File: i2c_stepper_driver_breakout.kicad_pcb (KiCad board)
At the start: 2 copper layers, 13 parts, among them J1 Conn_01x10, J2 Conn_01x10, J3 S4B-PH-SM4-TB, U1 PCA9629A, U2 A3909

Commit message: Continued layout
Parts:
- added U3: MAX17291, Locator_Footprints:MAX17291ATA+T, F.Cu at (140.8, 96.6)
- J1, J2: moved to B.Cu
- J3: value S4B-PH-SM4-TB -> B4B-PH-K-S; footprint Connector_JST:JST_PH_B4B-PH-K_1x04_P2.00mm_Vertical -> Locator_Footprints:JST_PH_S4B-PH-SM4-TB_1x04-1MP_P2.00mm_Horizontal; moved to B.Cu
- R1, R2: value 10K -> DNP
- U2: footprint Package_SO:MSOP-10-1EP_3x3mm_P0.5mm_EP1.73x1.98mm_ThermalVias -> Locator_Footprints:A3909
- moved R4 33.0 mm to (141.0, 103.8)
- moved R2 31.3 mm to (144.3, 109.5)
- moved C3 31.3 mm to (147.2, 109.5)
- moved R1 31.3 mm to (141.4, 109.5)
- moved C2 29.0 mm to (151.6, 105.5)
- moved C4 29.0 mm to (151.6, 108.5)
- moved C1 27.8 mm to (151.0, 92.6)
- moved R3 27.8 mm to (151.0, 90.6)
- moved J2 22.4 mm to (156.0, 108.3)
- moved J3 3.86 mm to (146.5, 88.2)
- moved U1 2.62 mm to (146.3, 104.2)
- moved U2 1.32 mm to (146.5, 94.4)
- moved J1 1.20 mm to (137.0, 85.4), turned to 180 degrees
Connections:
- J1 pad 1: Net-(J1-Pad1) -> GND
- J1 pad 10: Net-(J1-Pad10) -> GND
- J2 pad 1: Net-(J2-Pad1) -> GND
- J2 pad 10: Net-(J2-Pad10) -> GND
- U2 pad 11: (no net) -> GND
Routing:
- net /OUT3: track 0.00 -> 10.7 mm, vias 0 -> 2
- net /OUT2: track 0.00 -> 9.38 mm, vias 0 -> 2
- net /OUT1: track 0.00 -> 2.00 mm, vias 0 -> 2
- net /OUT4: track 0.00 -> 1.96 mm, vias 0 -> 2
- added copper zone on B.Cu, net GND
- added copper zone on F.Cu, net GND
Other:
- board outline added: 23 x 28 mm
- rule via_min_drill: 0.3 -> 0.2

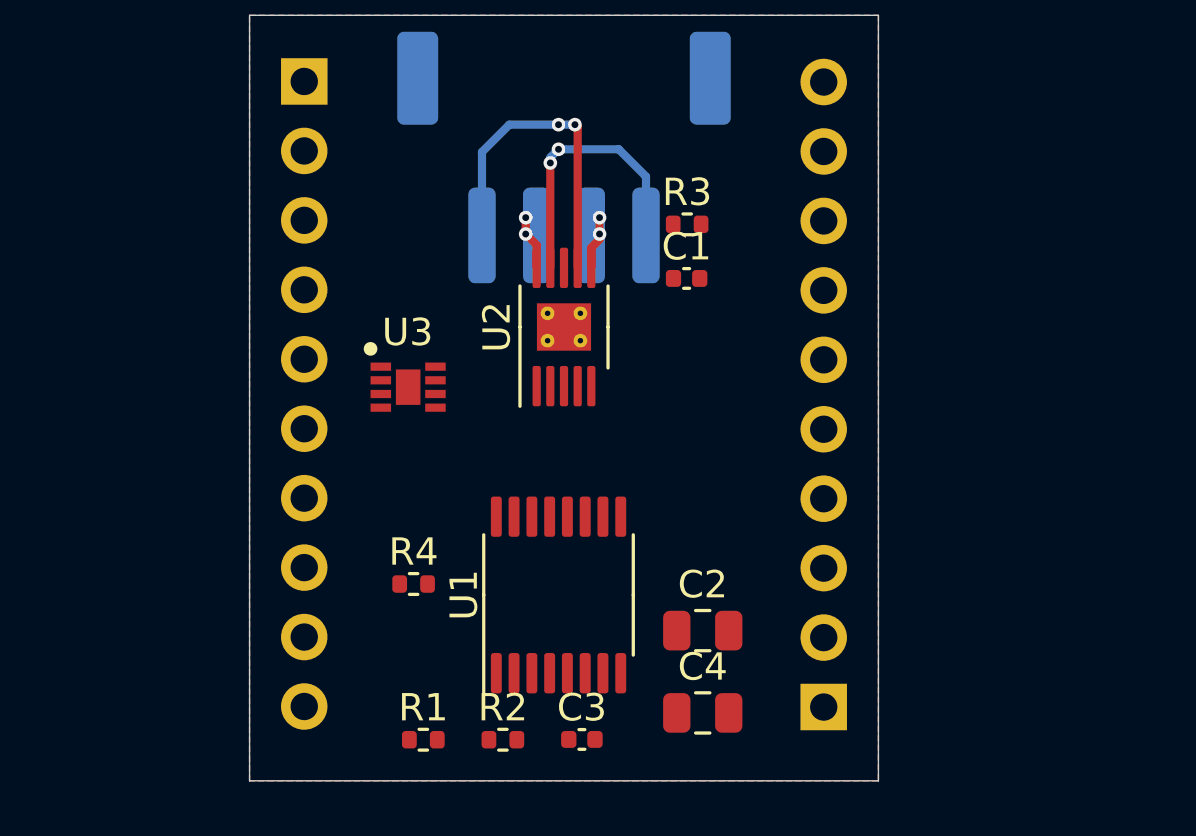
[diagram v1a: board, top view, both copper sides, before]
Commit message: Added boost converter, continued layout
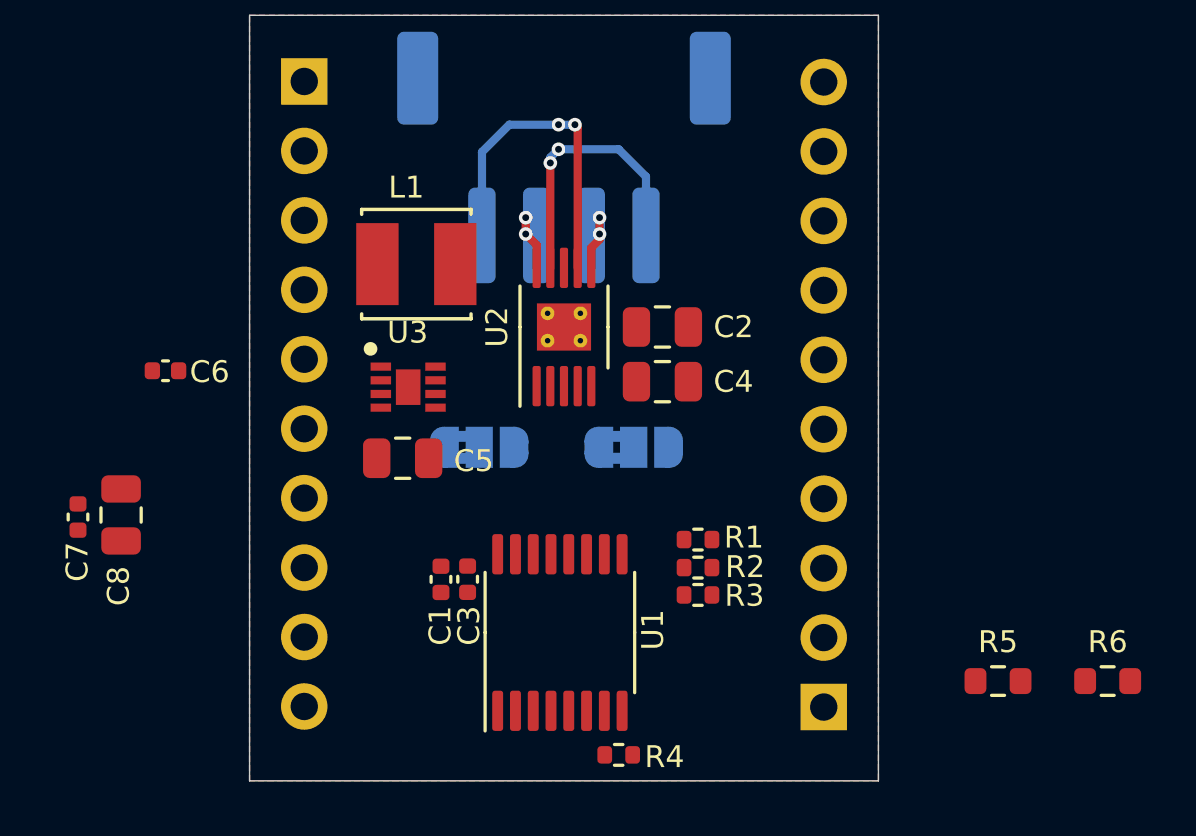
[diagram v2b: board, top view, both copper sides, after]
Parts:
- added C5: 22uF, Capacitor_SMD:C_0805_2012Metric, F.Cu at (140.6, 99.2)
- added C6: 1nF, Capacitor_SMD:C_0402_1005Metric, F.Cu at (131.9, 96.0)
- added C7: 100nF, Capacitor_SMD:C_0402_1005Metric, F.Cu at (128.7, 101.3)
- added C8: 22uF, Capacitor_SMD:C_0805_2012Metric, F.Cu at (130.3, 101.3)
- added JP1: VBB_Selection, Jumper:SolderJumper-3_P1.3mm_Bridged2Bar12_RoundedPad1.0x1.5mm, B.Cu at (143.4, 98.8)
- added JP2: VBB_Selection, Jumper:SolderJumper-3_P1.3mm_Bridged2Bar12_RoundedPad1.0x1.5mm, B.Cu at (149.1, 98.8)
- added L1: 4.7uH, Locator_Footprints:L_LQH44P, F.Cu at (141.1, 92.1)
- added R5: 1.4M, Resistor_SMD:R_0603_1608Metric, F.Cu at (162.4, 107.3)
- added R6: 412K, Resistor_SMD:R_0603_1608Metric, F.Cu at (166.4, 107.3)
- C2: value 20uF -> 22uF
- J3: value B4B-PH-K-S -> S4B-PH-SM4-TB
- moved C1 14.2 mm to (142.0, 103.6), turned to 270 degrees
- moved R3 13.6 mm to (151.4, 104.2), turned to 180 degrees
- moved R1 12.4 mm to (151.4, 102.2), turned to 180 degrees
- moved C4 12.2 mm to (150.1, 96.4)
- moved C2 11.2 mm to (150.1, 94.4)
- moved R4 9.76 mm to (148.5, 110.0)
- moved R2 9.52 mm to (151.4, 103.2), turned to 180 degrees
- moved C3 7.20 mm to (143.0, 103.6), turned to 270 degrees
- moved U1 1.38 mm to (146.3, 105.6)
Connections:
- net Net-(U3-Pad4) renamed /EN
- J1 pad 2: Net-(J1-Pad2) -> /OUT1
- J1 pad 3: Net-(J1-Pad3) -> /OUT2
- J2 pad 8: Net-(J2-Pad8) -> /OUT4
- J2 pad 9: Net-(J2-Pad9) -> /OUT3
- U3 pad 2: (no net) -> GND
- U3 pad 3: Net-(U3-Pad3) -> /VIN_BOOST
- U3 pad 7: Net-(U3-Pad7) -> /VOUT
- U3 pad 8: Net-(U3-Pad8) -> GND
- U3 pad 9: Net-(U3-Pad9) -> GND

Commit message: Finished schematic and layout for now
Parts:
- L1: footprint Locator_Footprints:L_LQH44P -> Inductor_SMD:L_1008_2520Metric
- R5, R6: footprint Resistor_SMD:R_0603_1608Metric -> Resistor_SMD:R_0402_1005Metric
- moved C7 20.9 mm to (148.9, 106.7), turned to 90 degrees
- moved C8 20.6 mm to (150.4, 105.9), turned to 90 degrees
- moved R6 18.6 mm to (147.9, 109.4), turned to 180 degrees
- moved C6 16.8 mm to (143.5, 108.2), turned to 180 degrees
- moved L1 14.0 mm to (142.4, 106.0)
- moved R5 13.1 mm to (149.4, 108.6), turned to 270 degrees
- moved R2 12.8 mm to (142.3, 94.2), turned to 0 degrees
- moved R1 12.8 mm to (142.3, 93.2), turned to 0 degrees
- moved U3 12.5 mm to (146.7, 107.6)
- moved JP1 10.5 mm to (152.9, 94.4), turned to 90 degrees
- moved JP2 10.1 mm to (140.0, 94.4), turned to 90 degrees
- moved R3 8.34 mm to (148.8, 96.3), turned to 270 degrees
- moved C5 8.23 mm to (146.8, 104.6)
- moved R4 7.96 mm to (148.9, 102.1), turned to 270 degrees
- moved C3 7.20 mm to (142.1, 96.5)
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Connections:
- J1 pad 10: GND -> /EN
- J1 pad 3: /OUT2 -> /OUT3
- J1 pad 4: Net-(J1-Pad4) -> /VIN_IC
- J1 pad 5: Net-(J1-Pad5) -> GND
- J1 pad 6: Net-(J1-Pad6) -> /P2
- J1 pad 7: Net-(J1-Pad7) -> /P1
- J1 pad 8: Net-(J1-Pad8) -> /P0
- J1 pad 9: Net-(J1-Pad9) -> /VIN_BOOST
- J2 pad 2: Net-(J2-Pad2) -> /RESET
- J2 pad 3: Net-(J2-Pad3) -> /SDA
- J2 pad 4: Net-(J2-Pad4) -> /SCL
- J2 pad 5: Net-(J2-Pad5) -> /INT
- J2 pad 6: Net-(J2-Pad6) -> GND
- J2 pad 7: Net-(J2-Pad7) -> /VIN_M
- J2 pad 9: /OUT3 -> /OUT2
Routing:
- net /VOUT: track 0.00 -> 34.4 mm, vias 0 -> 2
- net /VDD: track 0.00 -> 22.1 mm, vias 0 -> 3
- net /SDA: track 0.00 -> 18.0 mm
- net /SCL: track 0.00 -> 17.7 mm
- net /VIN_BOOST: track 0.00 -> 15.6 mm, vias 0 -> 2
- net /VBB: track 0.00 -> 14.7 mm, vias 0 -> 3
- net /OUT4: track 1.96 -> 16.2 mm, vias 2 -> 1
- net /INT: track 0.00 -> 12.4 mm
- net /OUT1: track 2.00 -> 14.4 mm
- net /RESET: track 0.00 -> 11.3 mm
- net /EN: track 0.00 -> 9.90 mm
- net /OUT2: track 9.38 -> 19.2 mm, vias 2 -> 1
- net /P2: track 0.00 -> 9.02 mm
- net /OUT3: track 10.7 -> 19.6 mm, vias 2 -> 1
- net /P1: track 0.00 -> 7.83 mm
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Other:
- net class Default: clearance 0.2 -> 0.1; trace_width 0.25 -> 0.15; via_drill 0.4 -> 0.35
- rule pad_to_mask_clearance: 0 -> 0.07
- rule trace_clearance: 0.2 -> 0.1
- rule trace_min: 0.2 -> 0.1
- rule via_min_drill: 0.2 -> 0.1
- board text added: "EN"
- board text added: "GND"
- board text added: "INT"
- board text added: "OUT1"
- board text added: "OUT2"
- board text added: "OUT3"
- board text added: "P0"
- board text added: "P1"
- board text added: "P2"
- board text added: "RST"
- board text added: "SCL"
- board text added: "SDA"
- board text added: "VIN"
- board text added: "VIN_IC"
- board text added: "VIN_M"

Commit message: Bugfixes
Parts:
- moved C2 1.05 mm to (150.1, 92.1)
- moved C4 1.05 mm to (152.1, 92.1)
- moved J2 0.67 mm to (156.7, 108.3)
- moved J1 0.64 mm to (136.4, 85.4)
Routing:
- net GND: track 6.97 -> 8.73 mm, vias 64 -> 59
- net /VIN_BOOST: track 15.6 -> 16.7 mm
- net /VBB: track 14.7 -> 13.8 mm
- net (no net): vias 0 -> 4
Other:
- board size 23 x 28 mm -> 24 x 28 mm
- net class Default: clearance 0.1 -> 0.15
- rule trace_clearance: 0.1 -> 0.15
- board text added: "OUT4"

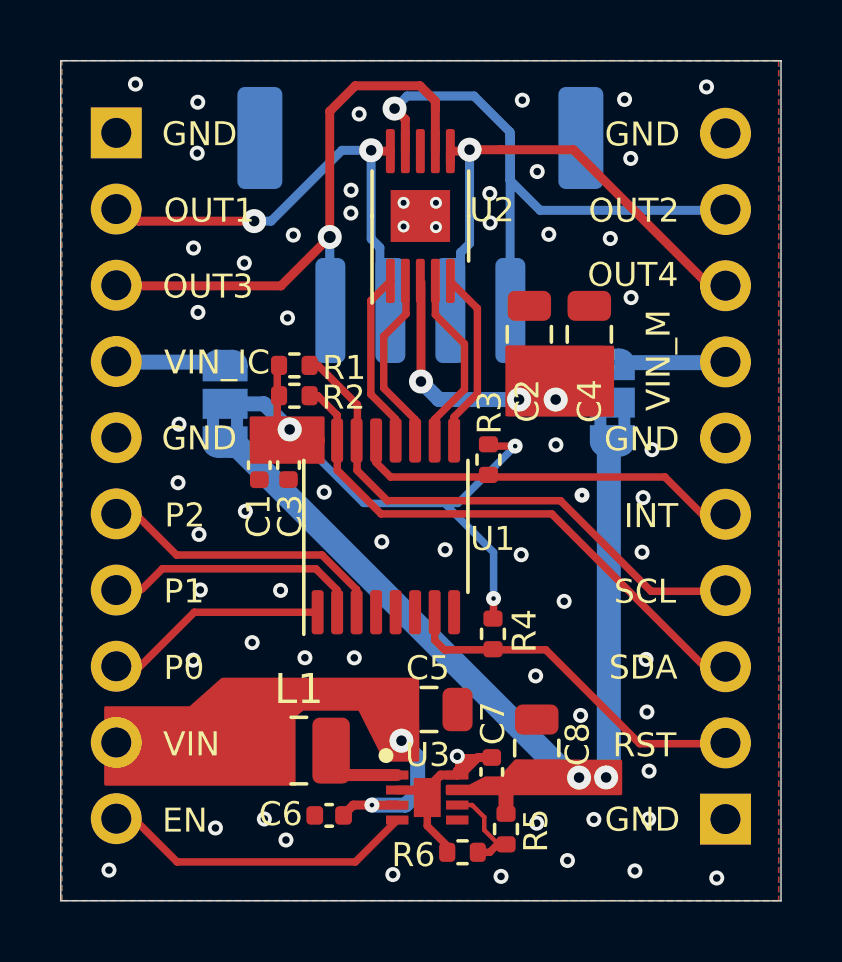
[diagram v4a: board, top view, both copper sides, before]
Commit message: Layout modifications due to some bugs
h
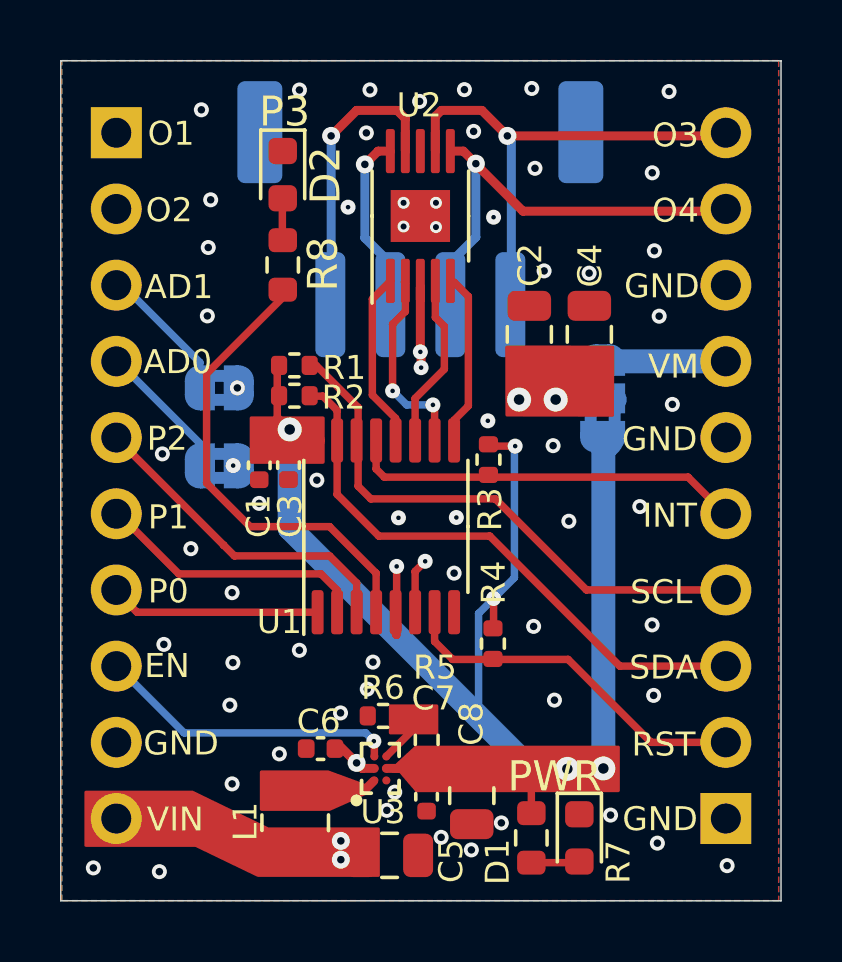
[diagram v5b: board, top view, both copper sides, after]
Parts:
- added D1: LED, LED_SMD:LED_0603_1608Metric, F.Cu at (151.8, 108.9)
- added D2: LED, LED_SMD:LED_0603_1608Metric, F.Cu at (141.9, 86.8)
- added G***: LOGO, Logos:skullbox_1200x1200, B.Cu at (146.2, 101.2)
- added JP3: SolderJumper_2_Bridged, Jumper:SolderJumper-2_P1.3mm_Bridged2Bar_RoundedPad1.0x1.5mm, B.Cu at (139.8, 96.5)
- added R7: 10K, Resistor_SMD:R_0603_1608Metric, F.Cu at (150.2, 108.9)
- added R8: 10K, Resistor_SMD:R_0603_1608Metric, F.Cu at (141.9, 89.8)
- JP2: value VBB_Selection -> SolderJumper_2_Bridged; footprint Jumper:SolderJumper-3_P1.3mm_Bridged2Bar12_RoundedPad1.0x1.5mm -> Jumper:SolderJumper-2_P1.3mm_Bridged2Bar_RoundedPad1.0x1.5mm
- U3: footprint Locator_Footprints:MAX17291ATA+T -> Locator_Footprints:MAX17291ATA+
- moved R6 5.26 mm to (145.3, 104.8)
- moved C5 5.04 mm to (145.5, 109.5)
- moved R5 3.98 mm to (146.7, 105.6), turned to 90 degrees
- moved C8 2.69 mm to (148.2, 107.5), turned to 270 degrees
- moved L1 2.41 mm to (142.3, 108.4), turned to 90 degrees
- moved C7 2.33 mm to (146.7, 107.5), turned to 270 degrees
- moved C6 2.24 mm to (143.2, 105.9)
- moved U3 1.84 mm to (145.2, 106.6), turned to 180 degrees
- moved JP2 0.56 mm to (139.8, 93.9), turned to 180 degrees
- moved JP1 0.35 mm to (152.6, 94.2)
- moved R4 0.33 mm to (148.9, 102.4)
- moved J3 0.19 mm to (146.5, 88.3)
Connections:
- net /VIN_M renamed /VM
- net Net-(U1-Pad12) renamed /O0
- net Net-(U1-Pad9) renamed /O3
- C1 pad 1: /VDD -> /VCC
- C3 pad 1: /VDD -> /VCC
- C5 pad 1: /VIN_BOOST -> /VIN
- C6 pad 1: /VIN_BOOST -> /VIN
- C7 pad 1: /VOUT -> /VCC
- C8 pad 1: /VOUT -> /VCC
- J1 pad 1: GND -> /OUT1
- J1 pad 10: /EN -> /VIN
- J1 pad 2: /OUT1 -> /OUT2
- J1 pad 3: /OUT3 -> /AD1
- J1 pad 4: /VIN_IC -> /AD0
- J1 pad 5: GND -> /P2
- J1 pad 6: /P2 -> /P1
- J1 pad 7: /P1 -> /P0
- J1 pad 8: /P0 -> /EN
- J1 pad 9: /VIN_BOOST -> GND
- J2 pad 10: GND -> /OUT3
- J2 pad 8: /OUT4 -> GND
- J2 pad 9: /OUT2 -> /OUT4
- J3 pad 1: /OUT3 -> /OUT2
- J3 pad 4: /OUT2 -> /OUT3
- JP1 pad 1: /VOUT -> /VCC
- JP2 pad 1: /VOUT -> GND
- JP2 pad 2: /VDD -> /AD1
- L1 pad 1: /VIN_BOOST -> /VIN
- R1 pad 1: /VDD -> /VCC
- R2 pad 1: /VDD -> /VCC
- R3 pad 1: /VDD -> /VCC
- R4 pad 1: /VDD -> /VCC
- R5 pad 1: /VOUT -> /VCC
- U1 pad 10: Net-(U1-Pad10) -> /O2
- U1 pad 11: Net-(U1-Pad11) -> /O1
- U1 pad 16: /VDD -> /VCC
- U1 pad 5: GND -> /AD0
- U1 pad 6: GND -> /AD1
- U2 pad 2: Net-(U1-Pad11) -> /O2
- U2 pad 4: Net-(U1-Pad10) -> /O1
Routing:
- net /VCC: track 0.00 -> 52.9 mm, vias 0 -> 5
- net /VOUT: track 34.4 -> 0.00 mm, vias 2 -> 0
- net /AD1: track 0.00 -> 22.2 mm, vias 0 -> 1
- net /VDD: track 22.1 -> 0.00 mm, vias 3 -> 0
- net /AD0: track 0.00 -> 19.8 mm, vias 0 -> 1
- net /VIN_BOOST: track 16.7 -> 0.00 mm, vias 2 -> 0
- net /P3: track 0.00 -> 15.8 mm
- net /VIN: track 0.00 -> 15.1 mm, vias 0 -> 3
- net GND: track 8.73 -> 0.00 mm, vias 59 -> 62
- net /O2: track 0.00 -> 6.56 mm, vias 0 -> 2
- net Net-(U1-Pad10): track 6.16 -> 0.00 mm
- net /O1: track 0.00 -> 5.81 mm
- net Net-(U1-Pad11): track 5.40 -> 0.00 mm
- net /VIN_IC: track 3.09 -> 0.00 mm
- net /OUT3: track 19.6 -> 16.6 mm
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- added copper zone on In1.Cu, net GND
- added copper zone on In2.Cu, net GND
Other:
- copper layers 2 -> 4
- net class Default: clearance 0.15 -> 0.1; via_dia 0.8 -> 0.6
- rule trace_clearance: 0.15 -> 0.1
- board text added: "AD0"
- board text added: "AD1"
- board text added: "JP1"
- board text added: "O1"
- board text added: "O2"
- board text added: "O3"
- board text added: "O4"
- board text added: "P3"
- board text added: "PCA9629A I²C Stepper Motor Controller"
- board text added: "PWR"
- board text added: "VCC"
- board text added: "VM"
- board text removed: "OUT1"
- board text removed: "OUT2"
- board text removed: "OUT3"
- board text removed: "OUT4"
- board text removed: "VIN_IC"
- board text removed: "VIN_M"
